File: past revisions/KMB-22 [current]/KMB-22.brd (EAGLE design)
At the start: 90.2 x 95.9 mm, 141 parts, among them J1 503182-1852, J2 10118194-0001LF, J3 DCJ0303, Q1 IRLML2803, Q10 IRLML5103, Q11 IRLML5103, Q12 IRLML5103, Q13 IRLML5103, Q14 IRLML2803, Q15 IRLML2803, Q16 IRLML5103, Q2 IRLML2803, Q5 IRLML2803, Q6 IRLML2803, Q7 IRLML2803, Q8 IRLML2803, Q9 IRLML5103, U1 MAX706R, U12 EP2W+, U13 RFM23BP, U14 S1216V8, U15 XTB_2018_07_15, U16 XTB_2018_07_15, U17 XTB_2018_07_15, U18 XTB_2018_07_15, U2 FXAS21002FXAS21002, U20 MR25H40MDF, U3 LSM9DS1, U4 ATSAMD21G-A, U5 MAX4372TEUK+T, U6 LTC4121-4.2, U7 TPS54226PWPRPWP14_2P31X2P46-L, U8 PE014006, U9 PE014006, X1 BU-SMA-V, X2 BU-SMA-V, X3 BU-SMA-V, Y1 32.768kHz

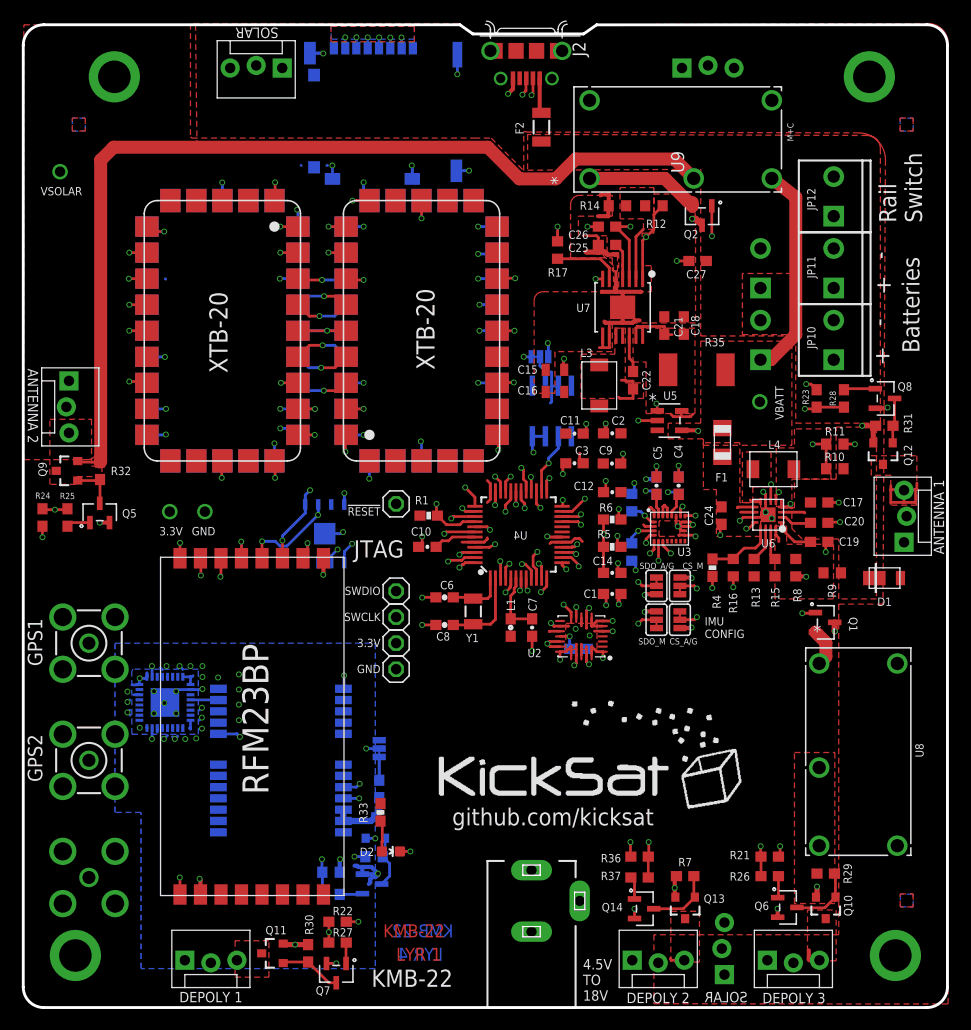
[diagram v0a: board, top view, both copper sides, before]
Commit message: changed solar panel connector on KMB-22
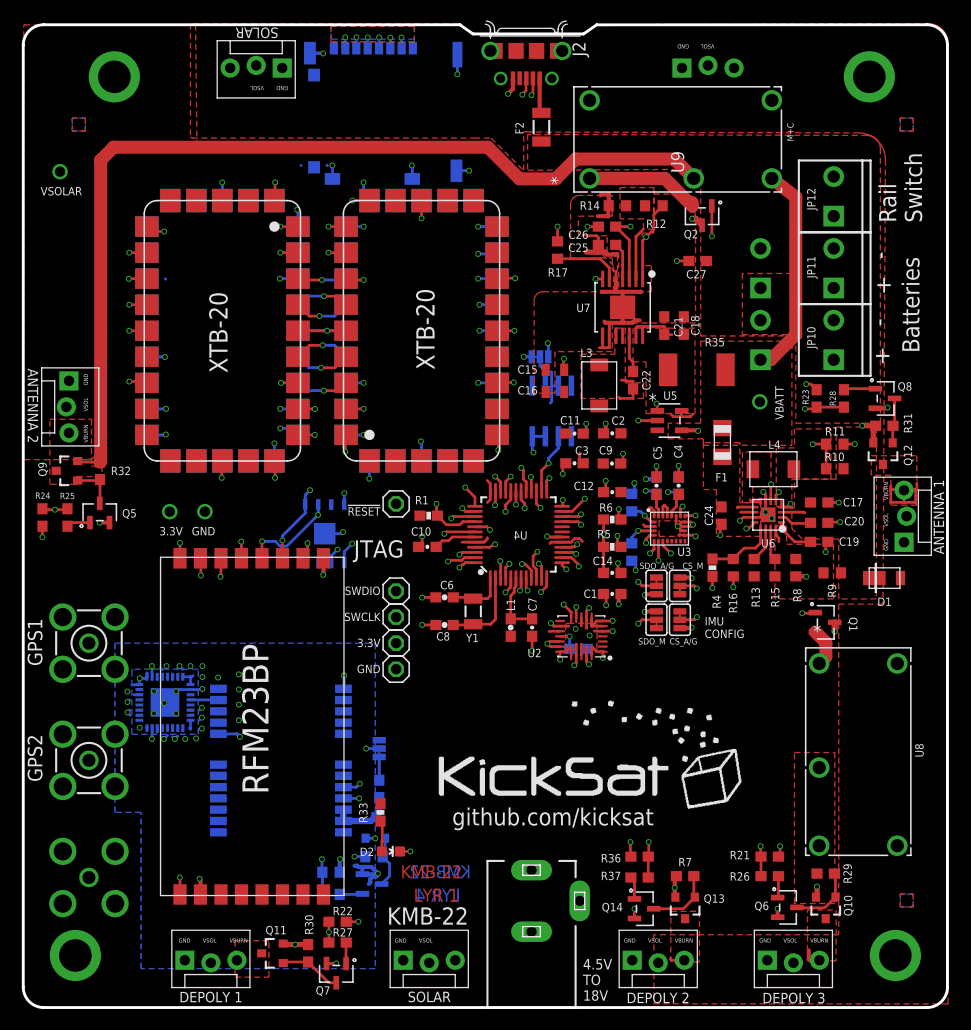
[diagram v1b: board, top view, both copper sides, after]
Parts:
- moved JP14 31.2 mm to (37.0, 4.50), flipped to the top, turned to 0 degrees
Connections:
- net 3.3V: now also U2.13
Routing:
- net VSOLAR: track 45.6 -> 47.1 mm
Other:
- board text added: "VBURN"
- board text added: "VSOL"
